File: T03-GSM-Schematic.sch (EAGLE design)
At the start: 19 parts, among them IC1 788TV, J1 POWER_JACKPTH_BREAD, J2 AVR, Q2 16M, U1 ATMEGA328P-PU

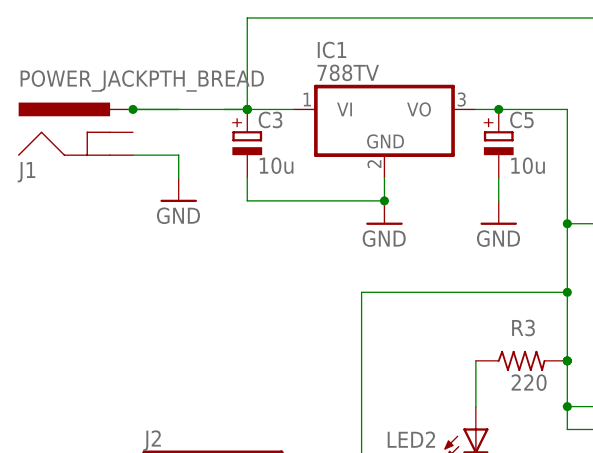
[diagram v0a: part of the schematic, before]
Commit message: fixed power jack connection
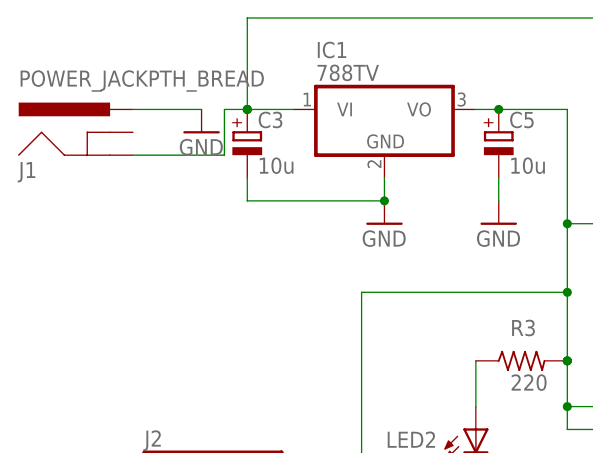
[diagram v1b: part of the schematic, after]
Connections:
- net 12V: now also J1.GND; no longer J1.PWR
- net GND: now also J1.PWR; no longer J1.GND
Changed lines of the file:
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@@
 <instance part="SV1" gate="1" x="269.24" y="167.64" rot="R180"/>
 <instance part="GND12" gate="1" x="271.78" y="182.88"/>
-<instance part="GND7" gate="1" x="152.4" y="195.58"/>
+<instance part="GND7" gate="1" x="154.94" y="203.2"/>
 </instances>
 <busses>
@@
 </segment>
 <segment>
-<pinref part="J1" gate="G$1" pin="GND"/>
+<pinref part="J1" gate="G$1" pin="PWR"/>
 <pinref part="GND7" gate="1" pin="GND"/>
-<wire x1="147.32" y1="200.66" x2="152.4" y2="200.66" width="0.1524" layer="91"/>
-<wire x1="152.4" y1="200.66" x2="152.4" y2="198.12" width="0.1524" layer="91"/>
+<wire x1="147.32" y1="205.74" x2="154.94" y2="205.74" width="0.1524" layer="91"/>
 </segment>
 </net>
@@
 <wire x1="157.48" y1="205.74" x2="160.02" y2="205.74" width="0.1524" layer="91"/>
 <pinref part="IC1" gate="A1" pin="VI"/>
-<wire x1="152.4" y1="205.74" x2="147.32" y2="205.74" width="0.1524" layer="91"/>
-<pinref part="J1" gate="G$1" pin="PWR"/>
-<wire x1="160.02" y1="205.74" x2="147.32" y2="205.74" width="0.1524" layer="91"/>
-<junction x="147.32" y="205.74"/>
-</segment>
-</net>
+<pinref part="J1" gate="G$1" pin="GND"/>
+<wire x1="147.32" y1="200.66" x2="157.48" y2="200.66" width="0.1524" layer="91"/>
+<wire x1="157.48" y1="200.66" x2="157.48" y2="205.74" width="0.1524" layer="91"/>
+</segment>
+</net>

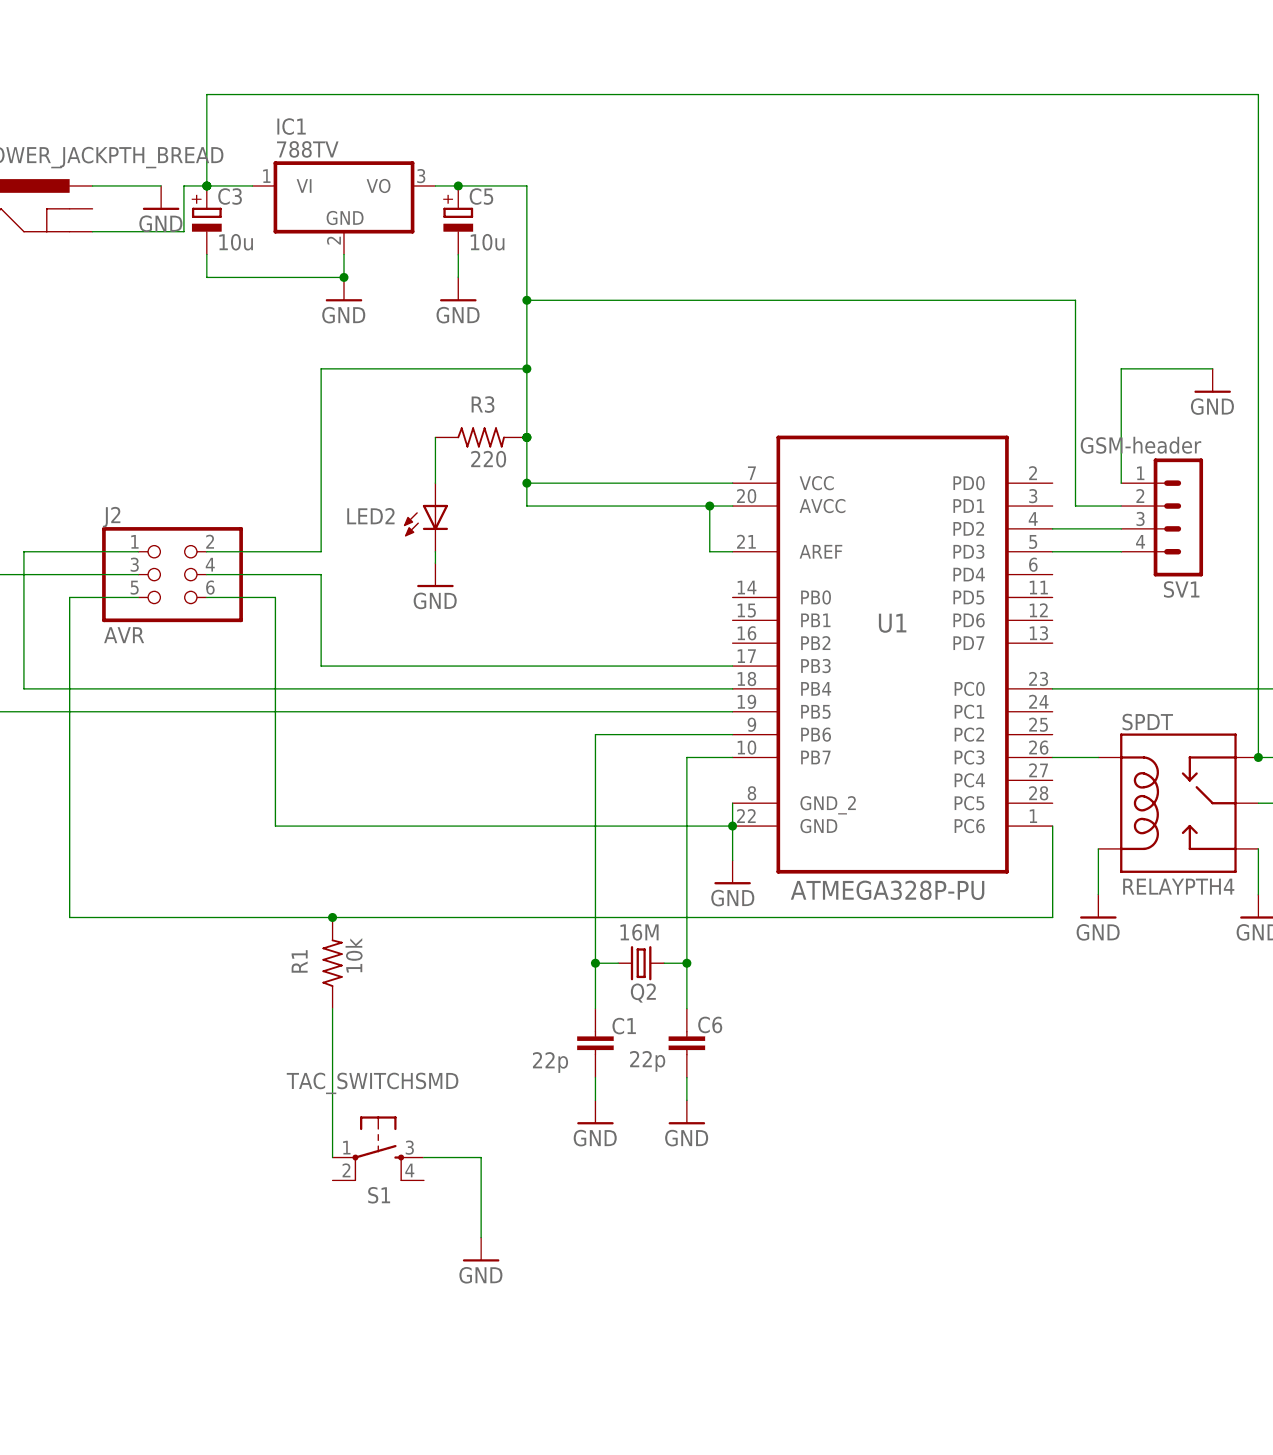
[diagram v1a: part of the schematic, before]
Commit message: Add files via upload
added flyback diode, bypass caps.  No board level work done yet.
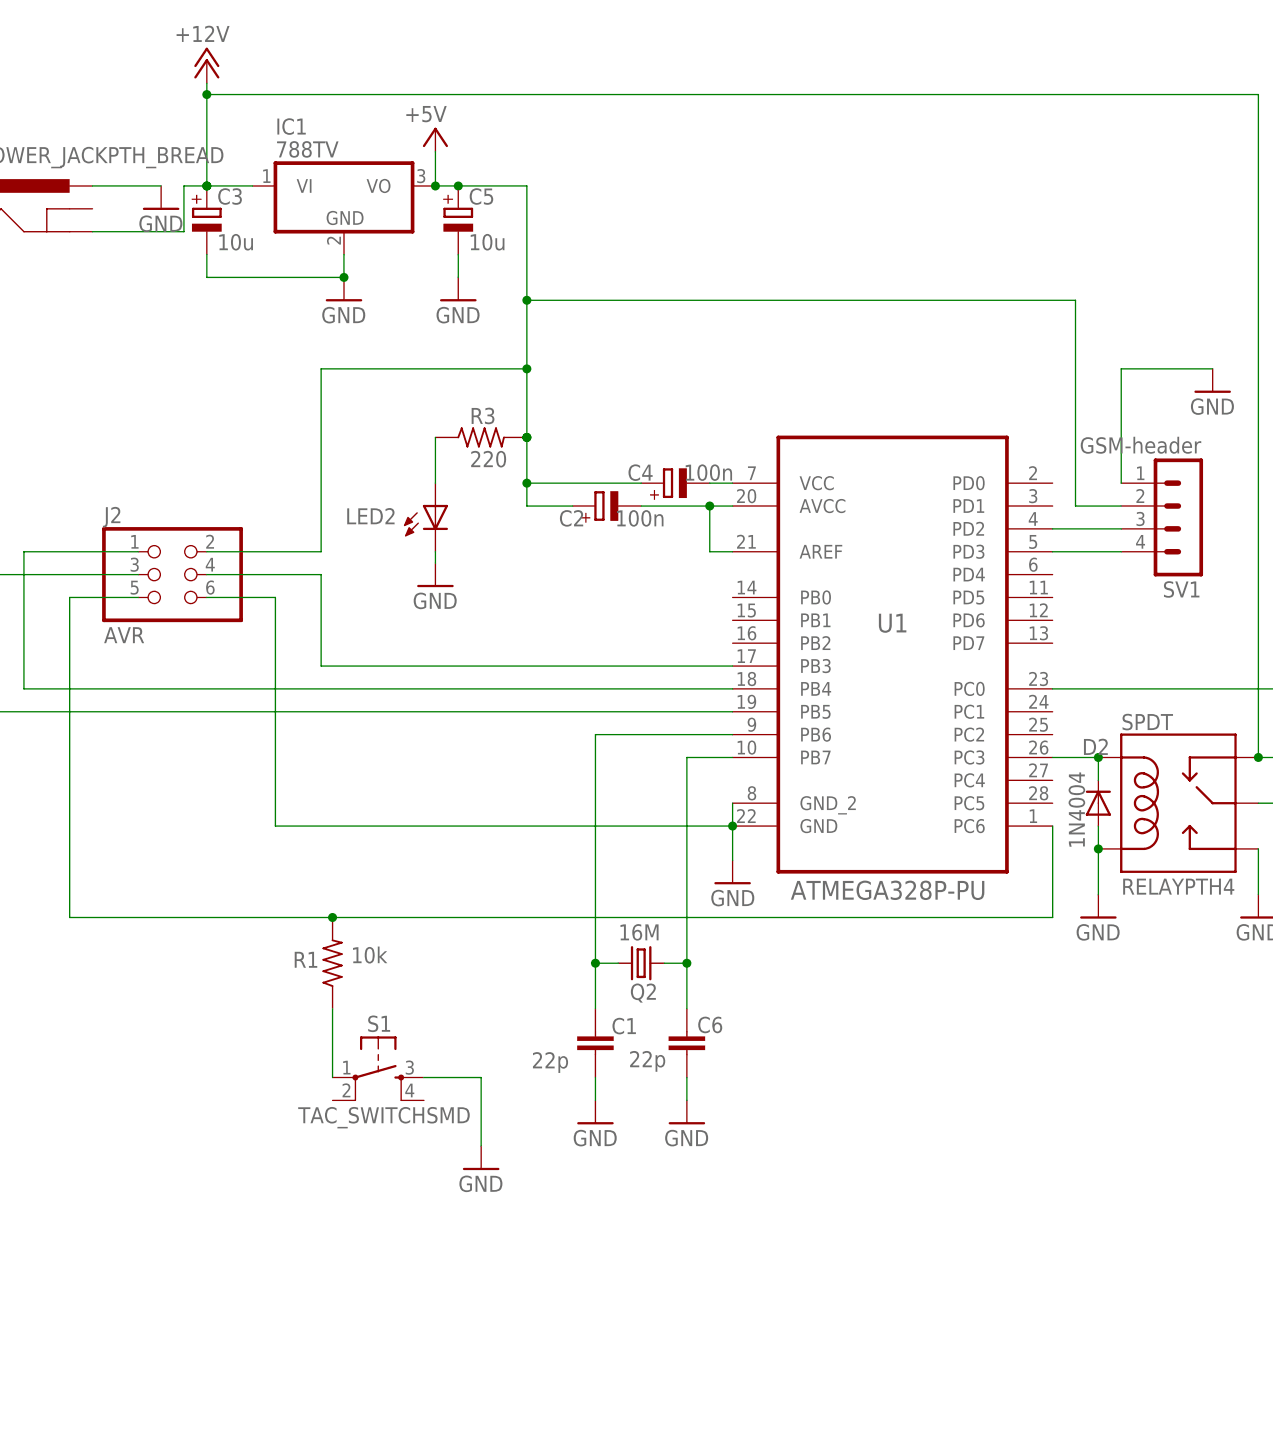
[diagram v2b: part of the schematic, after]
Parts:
- added C2, C4: 100n, rcl:CPOL-EUE5-10.5
- added D2: 1N4004, diode:1N4004
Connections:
- net 12V renamed +12V
- removed net 5V: C5.+, IC1.VO, J2.2, R3.2, SV1.2, U1.AREF, U1.AVCC, U1.VCC
- new net +5V: C2.+, C4.+, C5.+, IC1.VO, J2.2, R3.2, SV1.2
- new net N$1: C2.-, U1.AREF, U1.AVCC
- new net N$11: C4.-, U1.VCC
- net GND: now also D2.A
- net N$14: now also D2.C
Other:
- moved on the sheet: S1

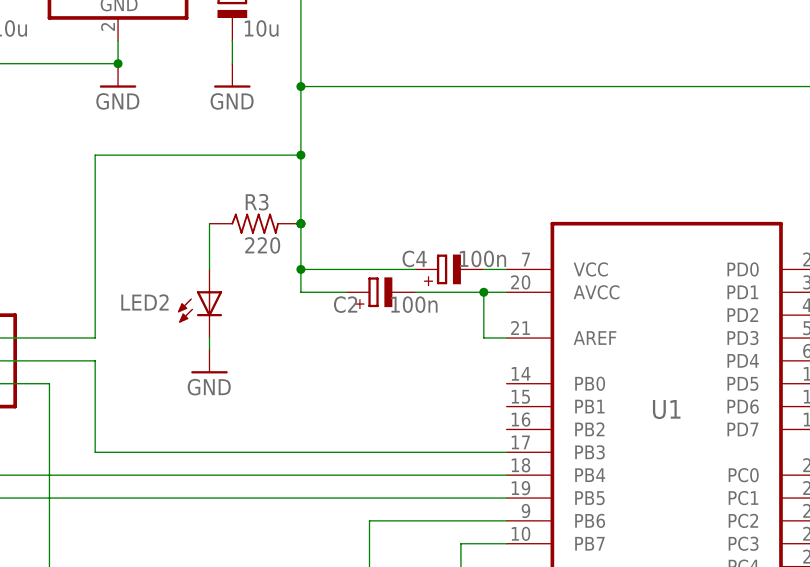
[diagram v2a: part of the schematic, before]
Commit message: Changed the layout of the PCB board
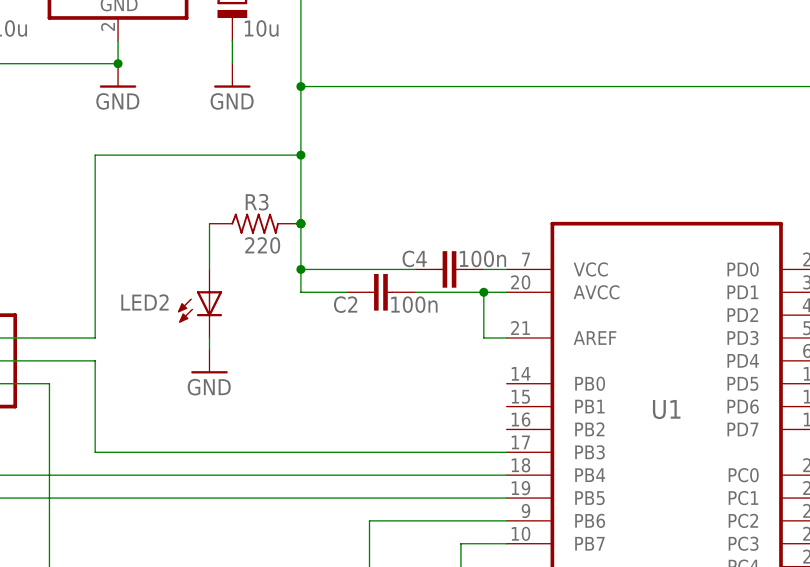
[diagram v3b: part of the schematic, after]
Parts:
- C2, C4: device rcl:CPOL-EUE5-10.5 -> rcl:C-EUC0603
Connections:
- net +5V: now also C2.1, C4.1; no longer C2.+, C4.+
- net N$1: now also C2.2; no longer C2.-
- net N$11: now also C4.2; no longer C4.-
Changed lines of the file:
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@@
 <?xml version="1.0" encoding="utf-8"?>
 <!DOCTYPE eagle SYSTEM "eagle.dtd">
-<eagle version="7.6.0">
+<eagle version="7.7.0">
 <drawing>
 <settings>
@@
 <setting verticaltext="up"/>
 </settings>
-<grid distance="0.05" unitdist="inch" unit="inch" style="lines" multiple="2" display="yes" altdistance="0.01" altunitdist="inch" altunit="inch"/>
+<grid distance="0.1" unitdist="inch" unit="inch" style="lines" multiple="1" display="no" altdistance="0.01" altunitdist="inch" altunit="inch"/>
 <layers>
 <layer number="1" name="Top" color="4" fill="1" visible="no" active="no"/>
@@
 <part name="GND12" library="supply1" deviceset="GND" device=""/>
 <part name="GND7" library="supply1" deviceset="GND" device=""/>
-<part name="C2" library="rcl" deviceset="CPOL-EU" device="E5-10.5" value="100n"/>
-<part name="C4" library="rcl" deviceset="CPOL-EU" device="E5-10.5" value="100n"/>
+<part name="C2" library="rcl" deviceset="C-EU" device="C0603" value="100n"/>
+<part name="C4" library="rcl" deviceset="C-EU" device="C0603" value="100n"/>
 <part name="D2" library="diode" deviceset="1N4004" device=""/>
 <part name="P+1" library="supply1" deviceset="+12V" device=""/>
@@
 <junction x="215.9" y="170.18"/>
 <wire x1="215.9" y1="170.18" x2="208.28" y2="170.18" width="0.1524" layer="91"/>
-<pinref part="C2" gate="G$1" pin="-"/>
+<pinref part="C2" gate="G$1" pin="2"/>
 </segment>
 </net>
@@
 <pinref part="U1" gate="A" pin="VCC"/>
 <wire x1="218.44" y1="172.72" x2="215.9" y2="172.72" width="0.1524" layer="91"/>
-<pinref part="C4" gate="G$1" pin="-"/>
+<pinref part="C4" gate="G$1" pin="2"/>
 </segment>
 </net>
@@
 <wire x1="256.54" y1="193.04" x2="195.58" y2="193.04" width="0.1524" layer="91"/>
 <junction x="195.58" y="193.04"/>
-<pinref part="C2" gate="G$1" pin="+"/>
-<pinref part="C4" gate="G$1" pin="+"/>
+<pinref part="C2" gate="G$1" pin="1"/>
+<pinref part="C4" gate="G$1" pin="1"/>
 <pinref part="P+2" gate="1" pin="+5V"/>
 <wire x1="185.42" y1="209.55" x2="185.42" y2="205.74" width="0.1524" layer="91"/>

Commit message: Add files via upload
Added test point, fixed ERC error.
More updates to come.
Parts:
- added R4: 0, rcl:R-US_0204/5
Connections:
- new net N$12: R4.2, U1.PC5
- net GND: now also R4.1
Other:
- moved on the sheet: D2, LED3, R2, SPDT

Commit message: Add files via upload
Added another test point after the voltage limiter and increased line thickness on power leads
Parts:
- added R5: 0, rcl:R-US_0204/5
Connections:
- net +5V: now also R5.2
- net GND: now also R5.1
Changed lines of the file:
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@@
 <part name="R4" library="rcl" deviceset="R-US_" device="0204/5" value="0"/>
 <part name="GND13" library="supply1" deviceset="GND" device=""/>
+<part name="R5" library="rcl" deviceset="R-US_" device="0204/5" value="0"/>
+<part name="GND14" library="supply1" deviceset="GND" device=""/>
 </parts>
 <sheets>
@@
 </instance>
 <instance part="GND13" gate="1" x="256.54" y="101.6"/>
+<instance part="R5" gate="G$1" x="200.66" y="203.2" smashed="yes" rot="R180">
+<attribute name="NAME" x="199.6186" y="199.39" size="1.778" layer="95"/>
+<attribute name="VALUE" x="200.152" y="205.74" size="1.778" layer="96"/>
+</instance>
+<instance part="GND14" gate="1" x="214.63" y="200.66"/>
 </instances>
 <busses>
@@
 <pinref part="GND13" gate="1" pin="GND"/>
 <wire x1="256.54" y1="110.49" x2="256.54" y2="104.14" width="0.1524" layer="91"/>
+</segment>
+<segment>
+<pinref part="R5" gate="G$1" pin="1"/>
+<pinref part="GND14" gate="1" pin="GND"/>
+<wire x1="214.63" y1="203.2" x2="205.74" y2="203.2" width="0.1524" layer="91"/>
 </segment>
 </net>
@@
 <segment>
 <wire x1="187.96" y1="205.74" x2="195.58" y2="205.74" width="0.1524" layer="91"/>
-<wire x1="195.58" y1="205.74" x2="195.58" y2="193.04" width="0.1524" layer="91"/>
+<wire x1="195.58" y1="205.74" x2="195.58" y2="203.2" width="0.1524" layer="91"/>
+<wire x1="195.58" y1="203.2" x2="195.58" y2="193.04" width="0.1524" layer="91"/>
 <wire x1="195.58" y1="193.04" x2="195.58" y2="185.42" width="0.1524" layer="91"/>
 <wire x1="195.58" y1="185.42" x2="195.58" y2="177.8" width="0.1524" layer="91"/>
@@
 <wire x1="185.42" y1="209.55" x2="185.42" y2="205.74" width="0.1524" layer="91"/>
 <junction x="185.42" y="205.74"/>
-</segment>
-</net>
+<pinref part="R5" gate="G$1" pin="2"/>
+<junction x="195.58" y="203.2"/>
+</segment>
+</net>
